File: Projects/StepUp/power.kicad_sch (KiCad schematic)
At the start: 0 parts

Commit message: feat(v8): Update to KiCAD v8, added boost converter
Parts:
- added U3: MIC2253, Package_DFN_QFN:DFN-12-1EP_3x3mm_P0.5mm_EP1.6x2.5mm_ThermalVias, symbol Regulator_Switching:MIC2253
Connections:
- new net: U3.13 (PGND), U3.5 (PGND), U3.6 (PGND)
- new net: U3.7 (SW), U3.8 (SW)
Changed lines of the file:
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@@
-(kicad_sch (version 20230121) (generator eeschema)
-  (paper "A4")
-  (title_block
-    (company "Samio")
-  )
+(kicad_sch
+	(version 20231120)
+	(generator "eeschema")
+	(generator_version "8.0")
+	(paper "A4")
+	(title_block
+		(company "Samio")
+	)
+	(symbol
+		(lib_id "Regulator_Switching:MIC2253")
+		(at 144.78 106.68 0)
+		(unit 1)
+		(exclude_from_sim no)
+		(in_bom yes)
+		(on_board yes)
+		(dnp no)
+		(fields_autoplaced yes)
+		(property "Reference" "U3"
+			(at 152.0541 91.44 0)
+			(effects
+				(font
+					(size 1.27 1.27)
+				)
+				(justify left)
+			)
+		)
+		(property "Value" "MIC2253"
+			(at 152.0541 93.98 0)
+			(effects
+				(font
+					(size 1.27 1.27)
+				)
+				(justify left)
+			)
+		)
+		(property "Footprint" "Package_DFN_QFN:DFN-12-1EP_3x3mm_P0.5mm_EP1.6x2.5mm_ThermalVias"
+			(at 144.78 106.68 0)
+			(effects
+				(font
+					(size 1.27 1.27)
+				)
+				(hide yes)
+			)
+		)
+		(property "Datasheet" "https://ww1.microchip.com/downloads/aemDocuments/documents/OTH/ProductDocuments/DataSheets/MIC2253-High-Current-1MHz-High-Efficiency-Boost-Regulator-with-OVP-and-Soft-Start-DS20006070A.pdf"
+			(at 144.78 106.68 0)
+			(effects
+				(font
+					(size 1.27 1.27)
+				)
+				(hide yes)
+			)
+		)
+		(property "Description" "3.5A 1 MHz boost regulator, 2.5V to 10V input, up to 30V output, DFN-12"
+			(at 144.78 106.68 0)
+			(effects
+				(font
+					(size 1.27 1.27)
+				)
+				(hide yes)
+			)
+		)
+		(pin "10"
+		)
+		(pin "5"
+		)
+		(pin "7"
+		)
+		(pin "9"
+		)
+		(pin "11"
+		)
+		(pin "12"
+		)
+		(pin "13"
+		)
+		(pin "1"
+		)
+		(pin "3"
+		)
+		(pin "6"
+		)
+		(pin "8"
+		)
+		(pin "2"
+		)
+		(pin "4"
+		)
+		(instances
+			(project "StepUp"
+				(path "/e0cca1c7-c263-49eb-8c40-74000ebe5285/e827d0b4-d448-43f9-95b8-3deddd7cd4ee"
+					(reference "U3")
+					(unit 1)
+				)
+			)
+		)
+	)
 )

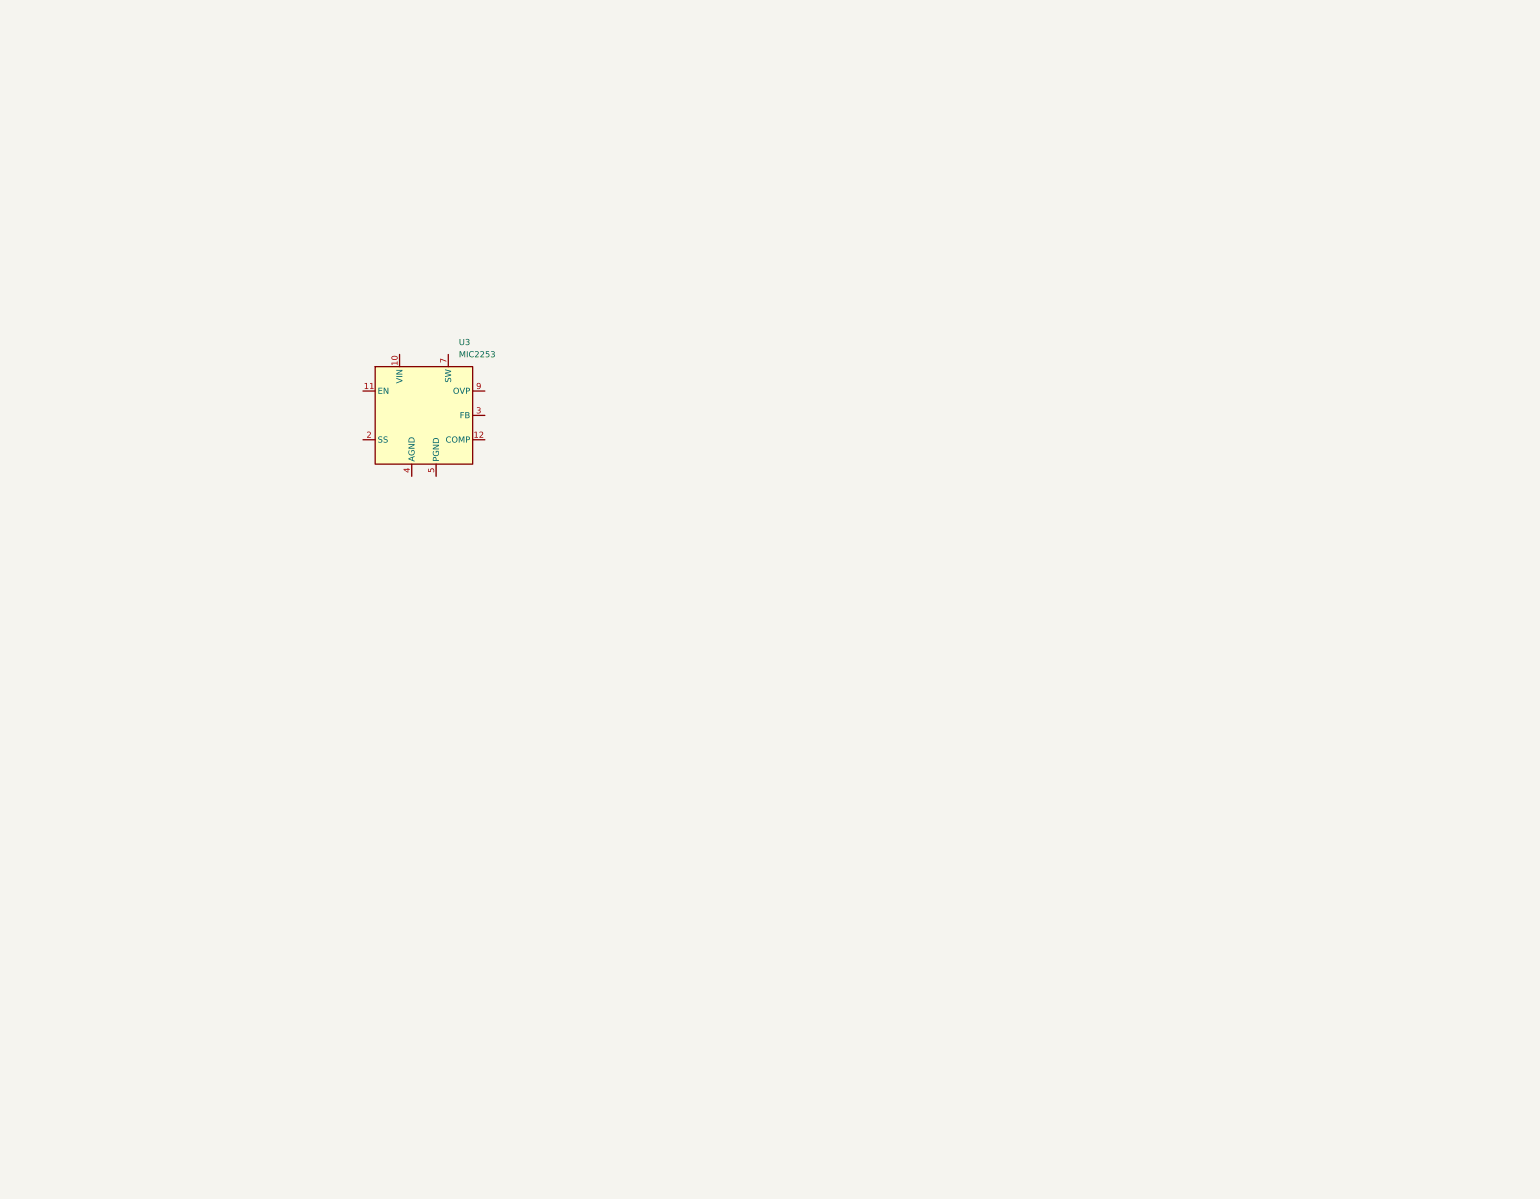
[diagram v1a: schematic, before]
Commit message: feat(rp2040): Layout begins, extra libraries
RPico minimal project downloaded + assets copied. Boost converter layout
in progress, 18650 battery holder added.
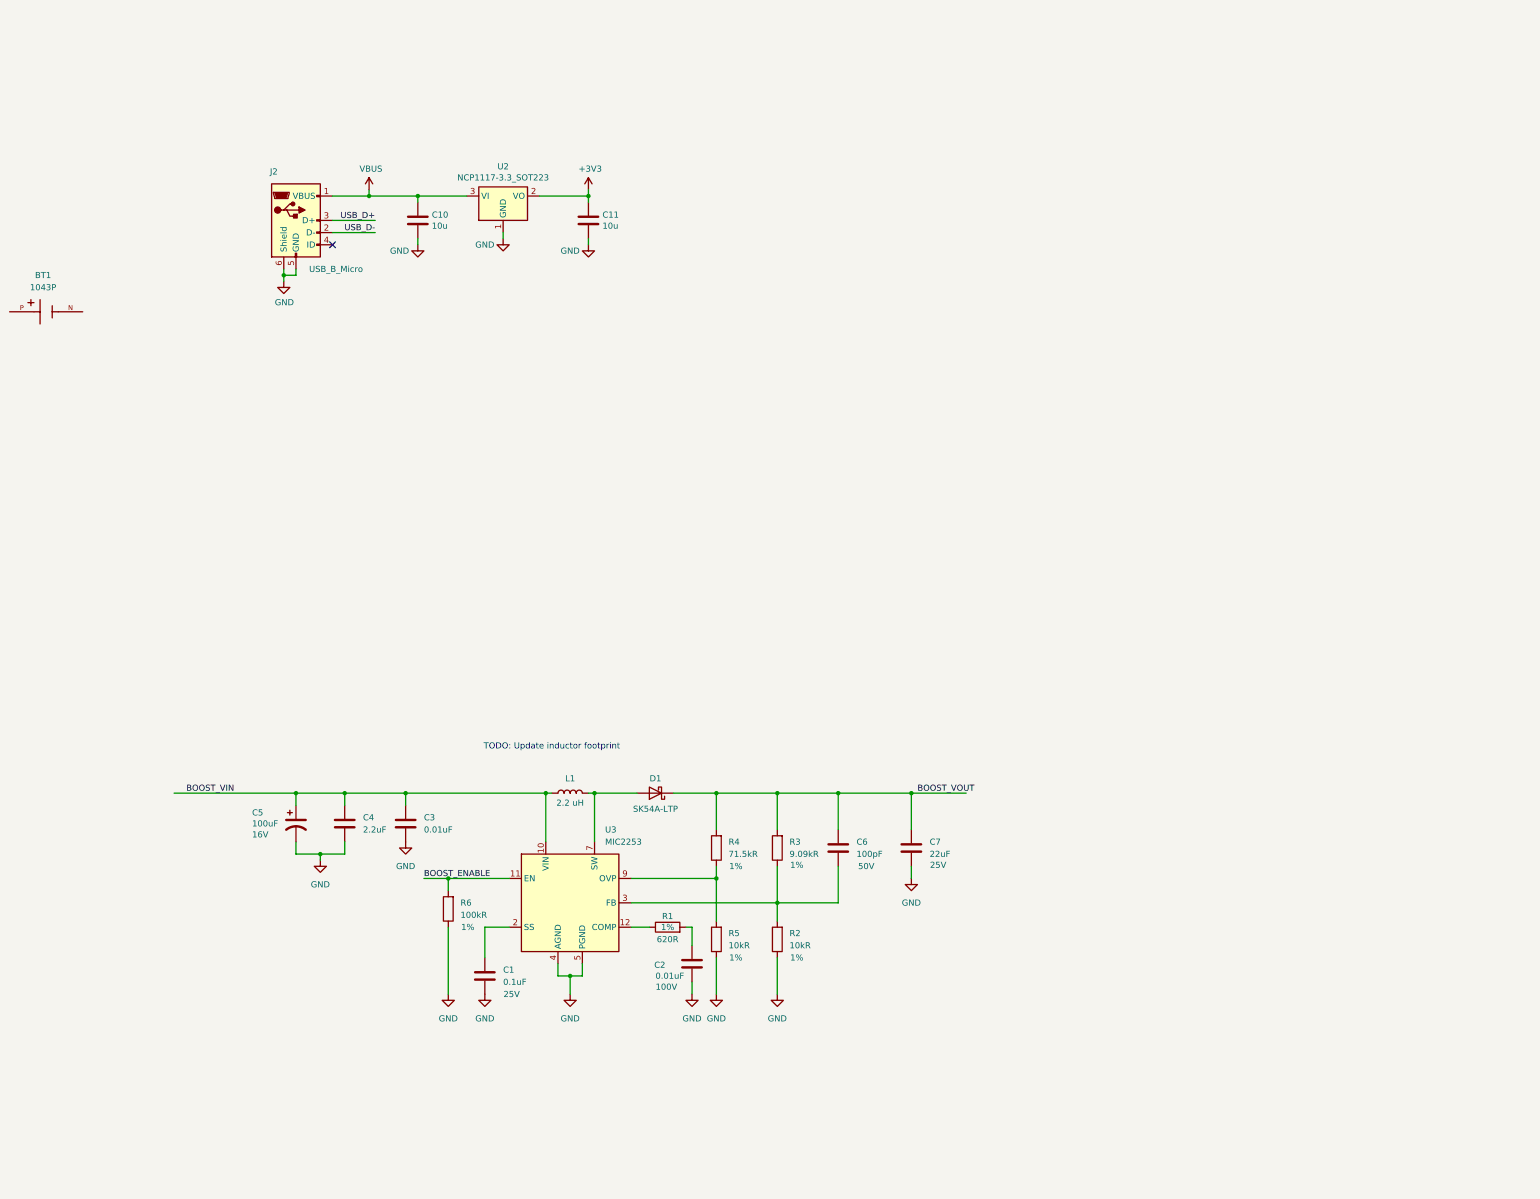
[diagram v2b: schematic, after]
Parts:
- added BT1: 1043P, Keystone:BAT_1043P, symbol 1043P:1043P
- added C1: 0.1uF, Capacitor_SMD:C_0603_1608Metric, symbol Device:C
- added C10, C11: 10u, Capacitor_SMD:C_0805_2012Metric, symbol Device:C
- added C2, C3: 0.01uF, Capacitor_SMD:C_0603_1608Metric, symbol Device:C
- added C4: 2.2uF, Capacitor_SMD:C_0603_1608Metric, symbol Device:C
- added C5: 100uF, Capacitor_Tantalum_SMD:CP_EIA-3528-12_Kemet-T, symbol Device:C_Polarized_US
- added C6: 100pF, Capacitor_SMD:C_0603_1608Metric, symbol Device:C
- added C7: 22uF, Capacitor_SMD:C_0805_2012Metric, symbol Device:C
- added D1: SK54A-LTP, Diode_SMD:D_SMA, symbol Device:D_Schottky
- added J2: USB_B_Micro, Connector_USB:USB_Micro-B_Amphenol_10103594-0001LF_Horizontal, symbol Connector:USB_B_Micro
- added L1: 2.2 uH, Inductor_SMD:L_Abracon_ASPI-4030S, symbol Device:L
- added R1: 620R, Resistor_SMD:R_0603_1608Metric, symbol Device:R
- added R2, R5: 10kR, Resistor_SMD:R_0603_1608Metric, symbol Device:R
- added R3: 9.09kR, Resistor_SMD:R_0603_1608Metric, symbol Device:R
- added R4: 71.5kR, Resistor_SMD:R_0603_1608Metric, symbol Device:R
- added R6: 100kR, Resistor_SMD:R_0603_1608Metric, symbol Device:R
- added U2: NCP1117-3.3_SOT223, Package_TO_SOT_SMD:SOT-223-3_TabPin2, symbol Regulator_Linear:NCP1117-3.3_SOT223
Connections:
- net BOOST_VIN: now reaches U3.10 (VIN)
- net BOOST_VIN: now also C3.1, C4.1, C5.1, L1.1
- net BOOST_ENABLE: now reaches U3.11 (EN)
- net BOOST_ENABLE: now also R6.2
- net at U3.12 (COMP): now also R1.1
- net GND: now reaches U3.13 (PGND), U3.5 (PGND), U3.6 (PGND)
- net GND: now also U3.4 (AGND), C1.2, C10.2, C11.2, C2.2, C3.2, C4.2, C5.2, C7.2, J2.5 (GND), J2.6 (Shield), R2.1, R5.1, R6.1, U2.1 (GND)
- net at U3.2 (SS): now also C1.1
- net at U3.3 (FB): now also C6.2, R2.2, R3.1
- net at U3.7 (SW), U3.8 (SW): now also D1.2 (A), L1.2
- net at U3.9 (OVP): now also R4.1, R5.2
- new net: C2.1, R1.2
- new net +3V3: C11.1, U2.2 (VO)
- new net BOOST_VOUT: C6.1, C7.1, D1.1 (K), R3.2, R4.2
- new net USB_D+: J2.3 (D+)
- new net USB_D-: J2.2 (D-)
- new net VBUS: C10.1, J2.1 (VBUS), U2.3 (VI)
- no-connect marks 0 -> 1
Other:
- note added: "TODO: Update inductor footprint"
- moved on the sheet: U3

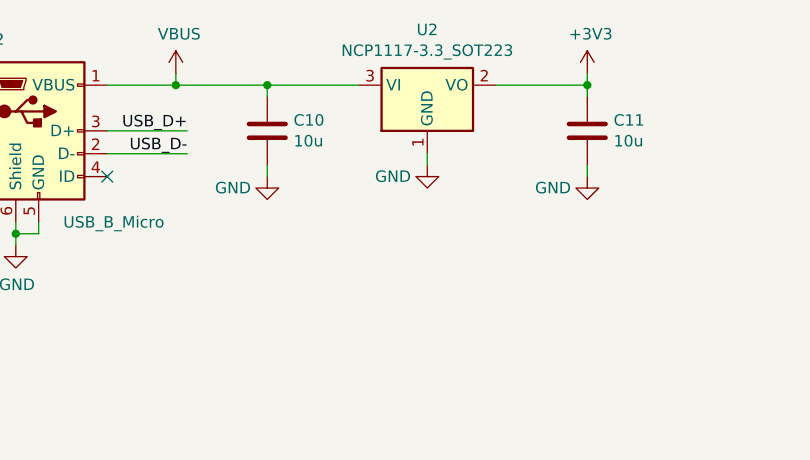
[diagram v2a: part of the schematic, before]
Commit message: feat(joystick): Added part
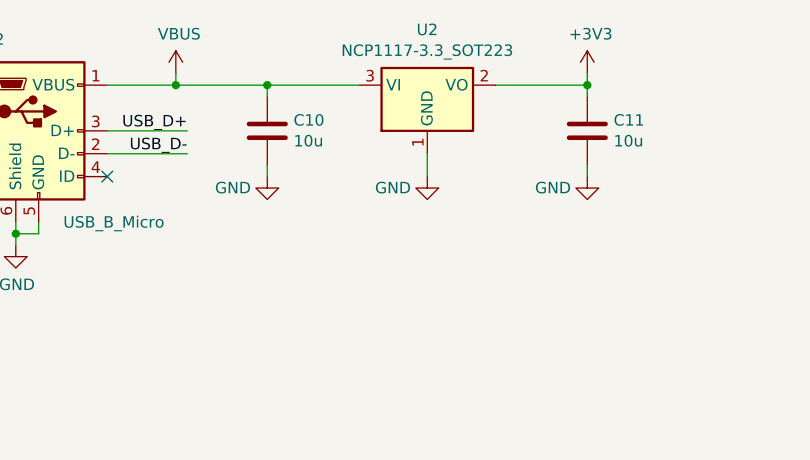
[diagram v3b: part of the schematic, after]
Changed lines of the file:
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@@
 	(wire
 		(pts
-			(xy 161.29 68.58) (xy 161.29 69.85)
+			(xy 161.29 68.58) (xy 161.29 71.12)
 		)
 		(stroke
@@
 	(symbol
 		(lib_id "power:GND")
-		(at 161.29 69.85 0)
+		(at 161.29 71.12 0)
 		(unit 1)
 		(exclude_from_sim no)
@@
 		(dnp no)
 		(property "Reference" "#PWR016"
-			(at 161.29 76.2 0)
+			(at 161.29 77.47 0)
 			(effects
 				(font
@@
 		)
 		(property "Value" "GND"
-			(at 157.48 71.12 0)
+			(at 157.48 72.39 0)
 			(effects
 				(font
@@
 		)
 		(property "Footprint" ""
-			(at 161.29 69.85 0)
+			(at 161.29 71.12 0)
 			(effects
 				(font
@@
 		)
 		(property "Datasheet" ""
-			(at 161.29 69.85 0)
+			(at 161.29 71.12 0)
 			(effects
 				(font
@@
 		)
 		(property "Description" ""
-			(at 161.29 69.85 0)
-			(effects
-				(font
+			(at 161.29 71.12 0)
+			(effects
+				(font

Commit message: feat(charge): Charge IC, USB ESD, sheet sections
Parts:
- added C24, C25: 4.7u, Capacitor_SMD:C_0805_2012Metric, symbol Device:C
- added D2: LED, LED_SMD:LED_0805_2012Metric, symbol Device:LED
- added R12: RProg, Resistor_SMD:R_0603_1608Metric, symbol Device:R
- added R13: Rled, Resistor_SMD:R_0603_1608Metric, symbol Device:R
- added U7: MCP73832T-2ACI_OT, digikey-footprints:SOT-753, symbol dk_PMIC-Battery-Chargers:MCP73832T-2ACI_OT
- added U8: USBLC6-2SC6, Package_TO_SOT_SMD:SOT-23-6, symbol Power_Protection:USBLC6-2SC6
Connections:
- net GND: now also BT1.N, C24.1, C25.2, R12.1, U7.2 (VSS), U8.2 (GND)
- net USB_D+: now also U8.6 (I/O1); no longer J2.3 (D+)
- net USB_D-: now also U8.4 (I/O2); no longer J2.2 (D-)
- net VBUS: now also C24.2, D2.2 (A), U7.4 (VDD), U8.5 (VBUS)
- net Vbat: now reaches BT1.P
- net Vbat: now also C25.1, U7.3 (VBAT)
- new net: R12.2, U7.5 (PROG)
- new net: R13.1, U7.1 (STAT)
- new net: D2.1 (K), R13.2
- new net USB_D+_IN: J2.3 (D+), U8.1 (I/O1)
- new net USB_D-_IN: J2.2 (D-), U8.3 (I/O2)
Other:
- note added: "Battery charge IC"
- note added: "Step up boost converter"
- note added: "USB input & 3v3 LDO"
- moved on the sheet: BT1, C1, C10, C11, C2, C3, C4, C5, C6, C7, D1, J2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
